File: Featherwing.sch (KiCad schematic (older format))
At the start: 22 parts, among them J11 GS3, J2 CONN_01X16, J3 CONN_01X12, J5 GROVE-CONNECTOR-SMD-90D(4+2P-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, J9 JST6, U2 ROF-78E

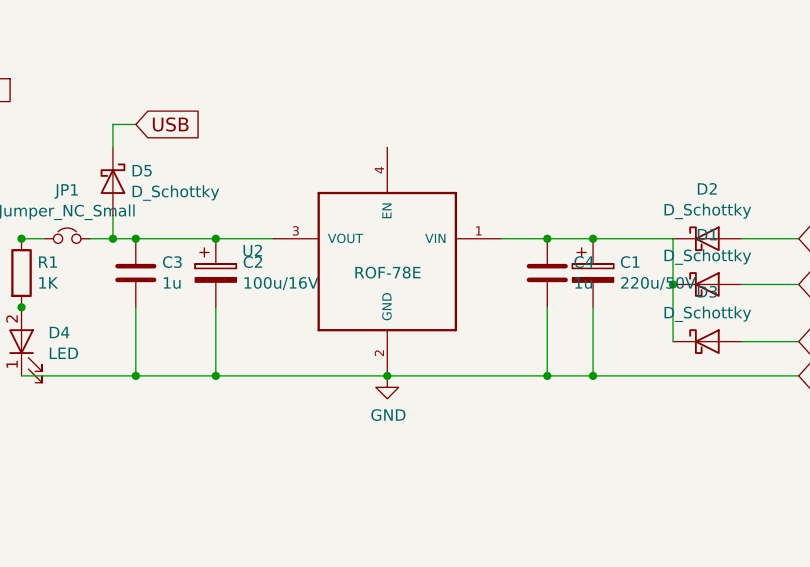
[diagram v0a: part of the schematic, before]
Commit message: Added more part numbers
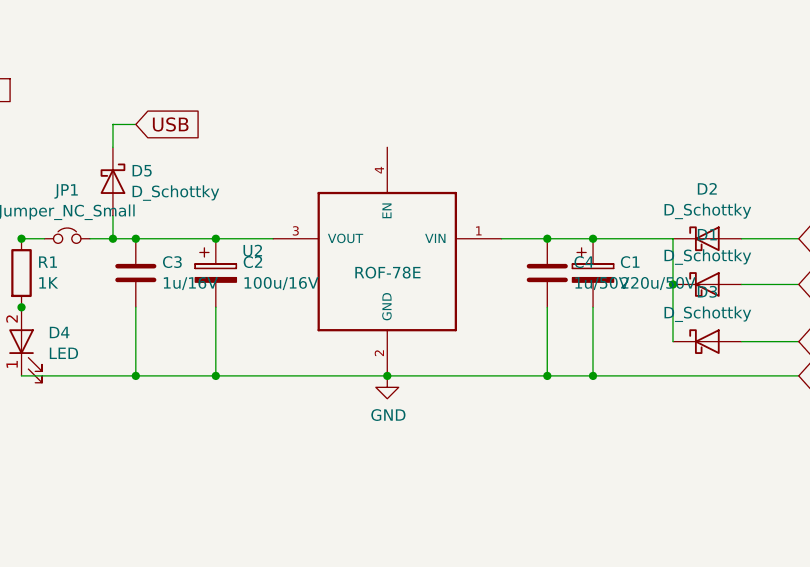
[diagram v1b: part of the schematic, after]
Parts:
- C1: manf# (none) -> UCM1H221MNL1GS
- C3: value 1u -> 1u/16V; manf# (none) -> 0603YD105KAT2A
- C4: value 1u -> 1u/50V; manf# (none) -> UMK107BJ105KA-T
- R1: manf# (none) -> CRG0603F1K0
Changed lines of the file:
@@
 F 2 "Capacitors_SMD:CP_Elec_8x10" H 288 -250 50  0001 C CNN
 F 3 "" H 250 -100 50  0001 C CNN
+F 4 "UCM1H221MNL1GS" H 7700 3050 60  0001 C CNN "manf#"
 	1    7700 3050
 	1    0    0    -1
@@
 P 5700 3050
 F 0 "C3" H 5815 3096 50  0000 L CNN
-F 1 "1u" H 5815 3005 50  0000 L CNN
+F 1 "1u/16V" H 5815 3005 50  0000 L CNN
 F 2 "Capacitors_SMD:C_0603" H 288 0   50  0001 C CNN
 F 3 "" H 250 150 50  0001 C CNN
+F 4 "0603YD105KAT2A" H 5700 3050 60  0001 C CNN "manf#"
 	1    5700 3050
 	1    0    0    -1
@@
 P 7500 3050
 F 0 "C4" H 7615 3096 50  0000 L CNN
-F 1 "1u" H 7615 3005 50  0000 L CNN
+F 1 "1u/50V" H 7615 3005 50  0000 L CNN
 F 2 "Capacitors_SMD:C_0603" H 2088 0   50  0001 C CNN
 F 3 "" H 2050 150 50  0001 C CNN
+F 4 "UMK107BJ105KA-T" H 7500 3050 60  0001 C CNN "manf#"
 	1    7500 3050
 	1    0    0    -1
@@
 F 2 "Resistors_SMD:R_0603_HandSoldering" V -70 150 50  0001 C CNN
 F 3 "" H 0   150 50  0001 C CNN
+F 4 "CRG0603F1K0" H 5200 3050 60  0001 C CNN "manf#"
 	1    5200 3050
 	1    0    0    -1

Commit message: JST parts
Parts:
- J9: manf# (none) -> SM06B-SRSS-TB(LF)(SN)
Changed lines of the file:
@@
 F 2 "Connectors_JST:JST_SH_SM06B-SRSS-TB_06x1.00mm_Angled" H 0   -150 50  0001 C CNN
 F 3 "" H 0   -150 50  0001 C CNN
+F 4 "SM06B-SRSS-TB(LF)(SN)" H 3600 4400 60  0001 C CNN "manf#"
 	1    3600 4400
 	-1   0    0    1
